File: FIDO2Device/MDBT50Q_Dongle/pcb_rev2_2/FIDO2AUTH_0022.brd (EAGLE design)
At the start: 19.5 x 34.3 mm, 40 parts, among them CN1 TE-1734028, CN2 IF_5PIN_H, SW1 SKRPACE010, SW2 SKTADAE010, U1 MDBT50Q-P1M, U2 XC6206P302MR-G, U3 RV-3028-C7, X1 NX3215SA-32.768K

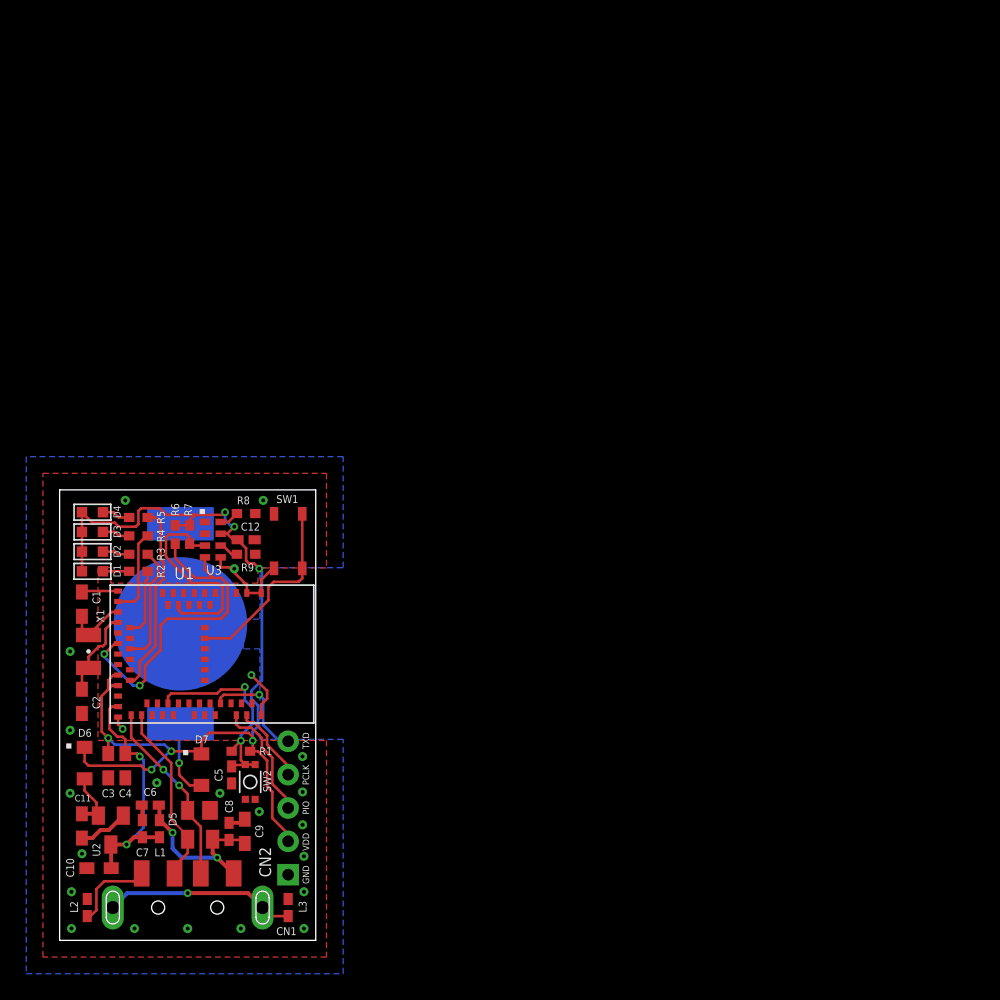
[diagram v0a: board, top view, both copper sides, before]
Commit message: 捨て板設定を追加
・認識マークを捨て板上に４点追加
・回路図を修正
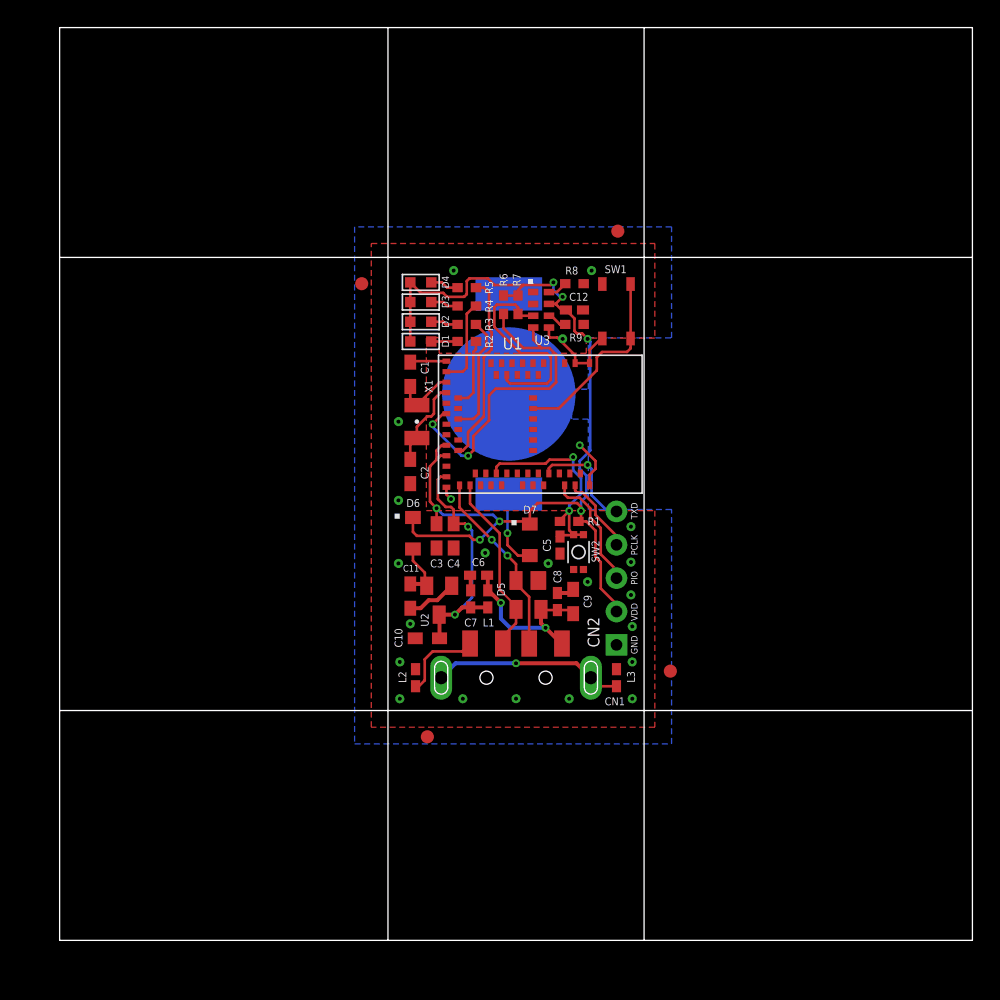
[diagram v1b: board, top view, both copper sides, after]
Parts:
- added P1, P2, P3, P4: 0, Generic:ROUND-MARK-1.0
- moved BAT1 30.5 mm to (34.2, 41.6)
- moved C12 30.5 mm to (39.2, 48.0)
- moved D5 30.5 mm to (35.7, 26.3)
- moved R8 30.5 mm to (39.2, 50.0)
- moved R9 30.5 mm to (39.2, 46.9)
- moved C1 30.5 mm to (26.7, 43.1)
- moved C10 30.5 mm to (28.0, 23.0)
- moved C11 30.5 mm to (26.7, 26.2)
- moved C2 30.5 mm to (26.7, 35.7)
- moved C3 30.5 mm to (28.7, 30.8)
- moved C4 30.5 mm to (30.0, 30.8)
- moved C5 30.5 mm to (38.1, 30.1)
- moved C6 30.5 mm to (31.9, 27.8)
- moved C7 30.5 mm to (31.3, 26.0)
- moved C8 30.5 mm to (37.9, 25.8)
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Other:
- board size 19.5 x 34.3 mm -> 69.5 x 69.5 mm

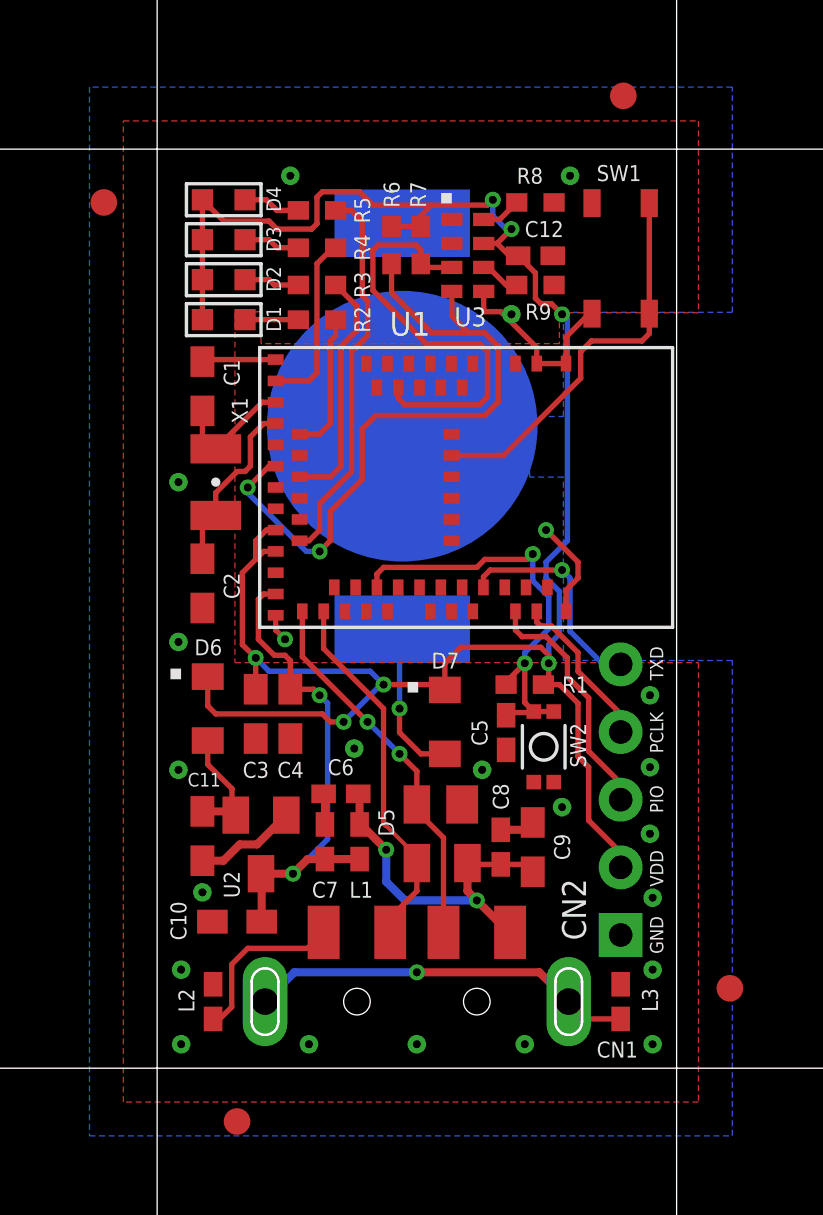
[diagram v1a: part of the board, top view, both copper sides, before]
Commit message: 配線レイアウトを修正
・GNDビア位置を調整
・べたGND領域を調整
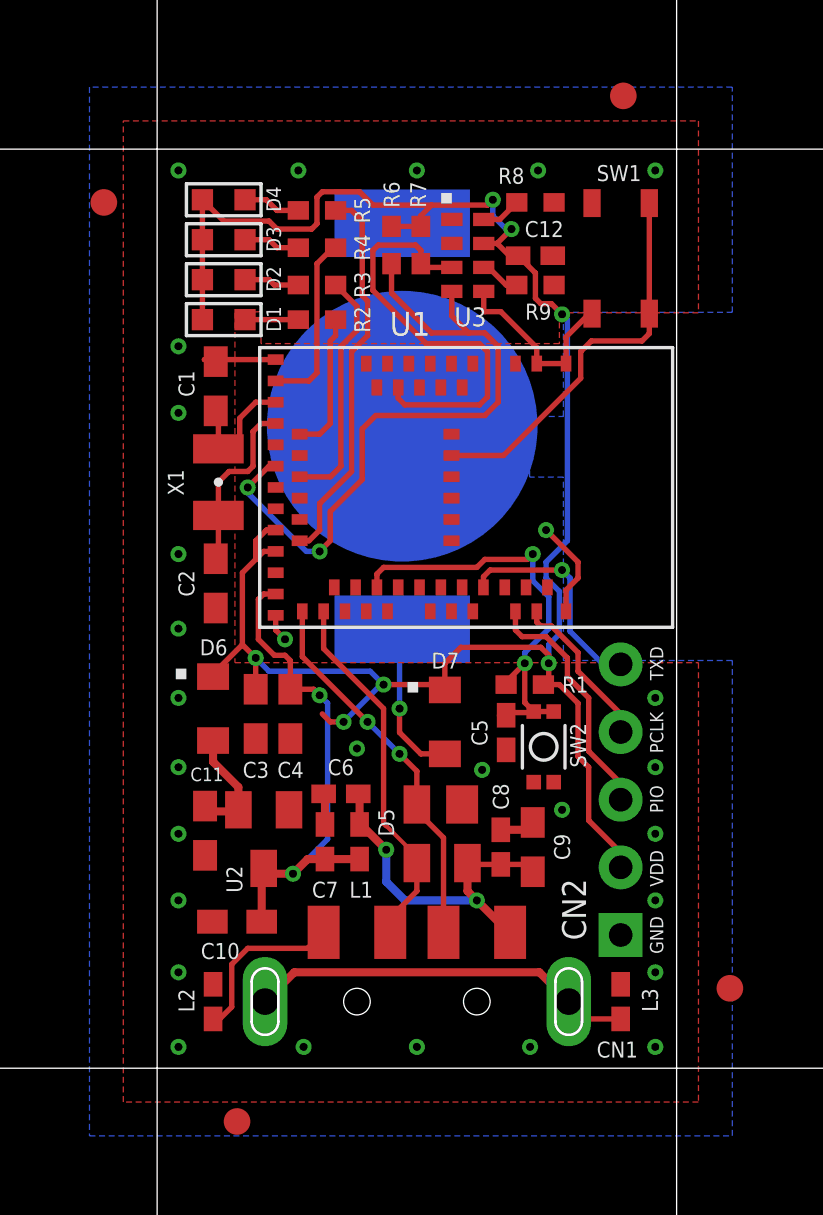
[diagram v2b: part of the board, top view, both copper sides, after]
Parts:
- moved C1 0.50 mm to (27.2, 43.1)
- moved C2 0.50 mm to (27.2, 35.7)
- moved U2 0.22 mm to (29.0, 26.1)
- moved C11 0.22 mm to (26.8, 26.4)
- moved D6 0.20 mm to (27.1, 31.0)
- moved X1 0.10 mm to (27.3, 39.5)
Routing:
- net VDD_NRF: track 78.9 -> 75.0 mm
- net 0V: track 21.2 -> 17.7 mm, vias 23 -> 29
- net N$3: vias 1 -> 0

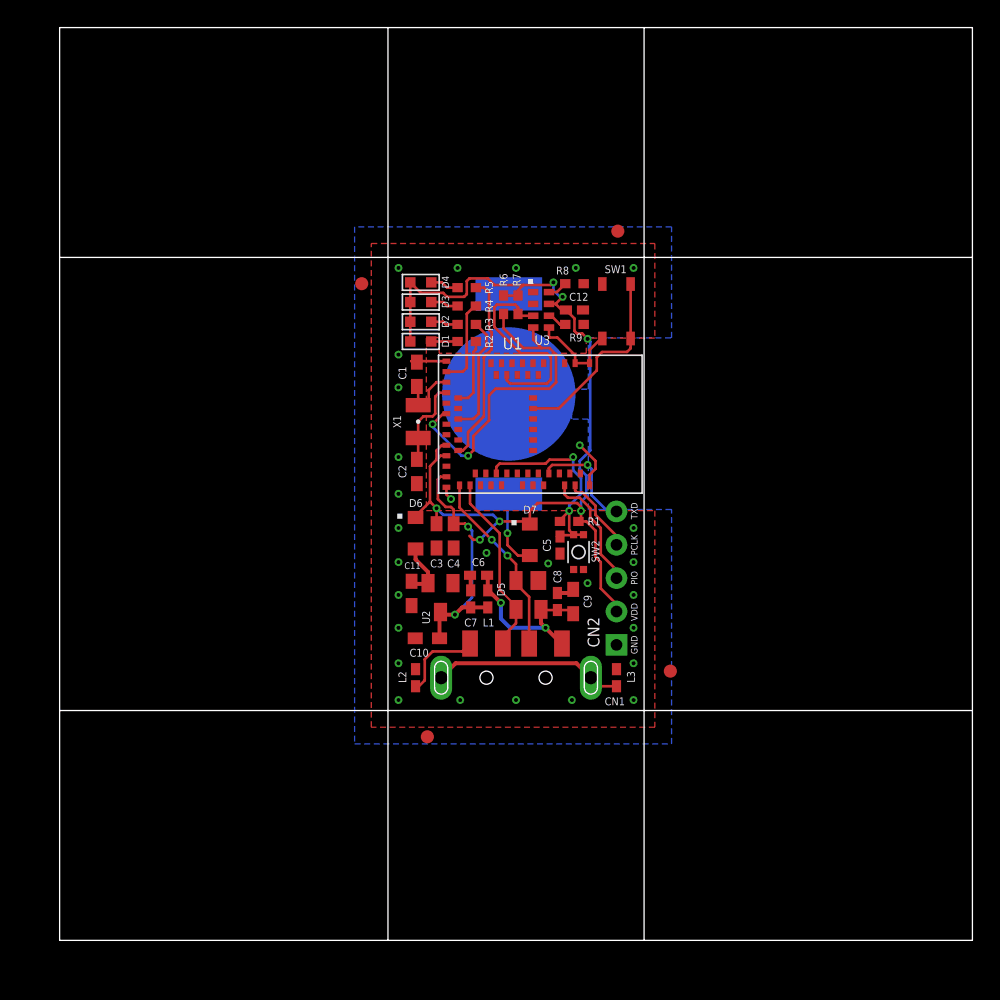
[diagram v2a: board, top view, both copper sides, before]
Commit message: バグ修正
・製造発注時、ガーバービュアーで外形線／Vカット線が参照できない不具合を解消
（前回発注時と同様、外形線の太さを0.2mmに修正）
・この修正に伴い、べたGNDの外側が切れてしまうため、一部部品を外形線から0.1mm以上オフセットさせるよう修正
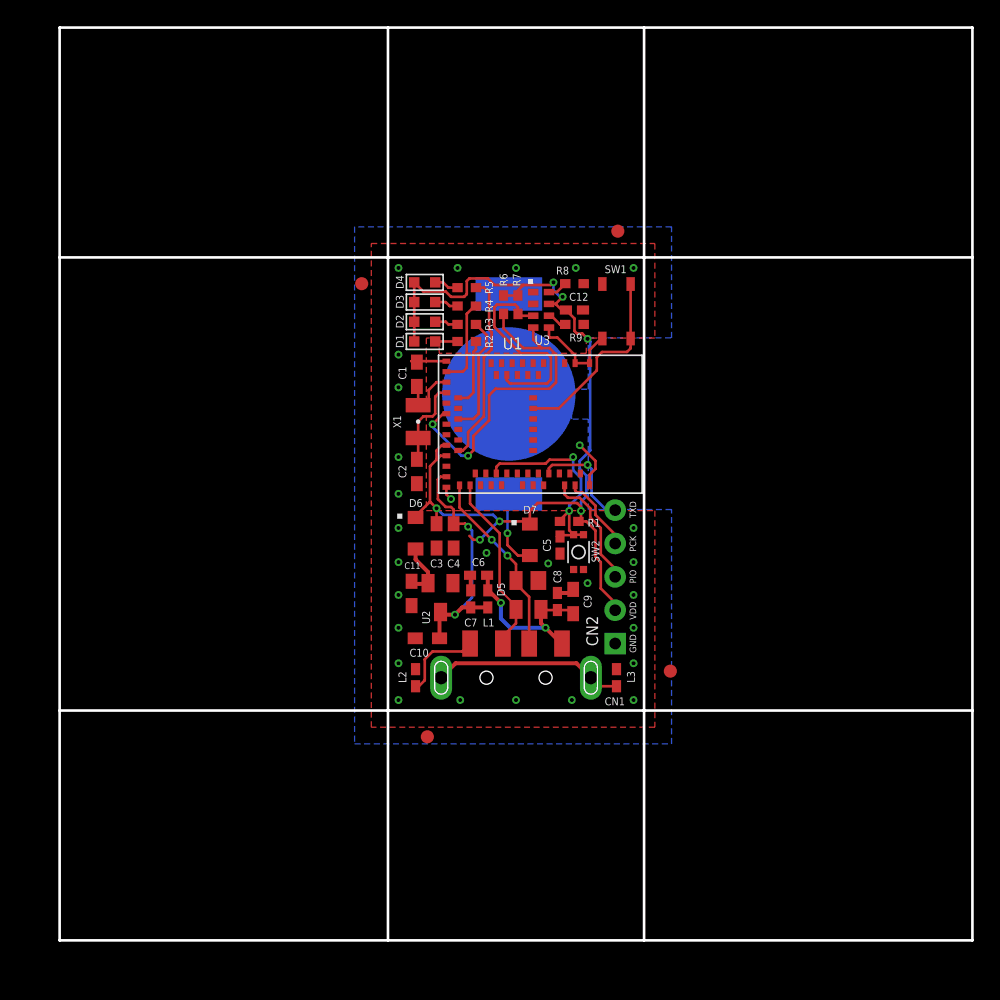
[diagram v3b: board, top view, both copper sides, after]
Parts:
- moved D1 0.30 mm to (27.8, 45.6)
- moved D2 0.30 mm to (27.8, 47.1)
- moved D3 0.30 mm to (27.8, 48.6)
- moved D4 0.30 mm to (27.8, 50.1)
- moved CN2 0.14 mm to (42.3, 22.6)
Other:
- board text added: "PCK"
- board text removed: "PCLK"
